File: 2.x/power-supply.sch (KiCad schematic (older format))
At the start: 46 parts, among them Q29 BC846, Q30 MOSFET_P, Q31 BSS138, U6 78L05, U7 AP1117IE33G, U8 ZXCT1107SA-7, U9 ZXCT1107SA-7

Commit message: Added RGB output and finished power supply monitor schematic, including new current monitor and voltage monitor divider values.
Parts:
- removed R128, R129, R131, R132, R133: R, ~, symbol R
- removed U9: ZXCT1107SA-7, symbol ZXCT1107SA-7
- added U9: ZXCT1086E5TA, ~, symbol ZXCT1086E5TA
- D35: value VSOL -> LED
- D36: value 12V -> LED
- D37: value 5V -> LED
- D38: value 3.3V -> LED
- Q30: value MOSFET_P -> FDD5614P
- R115: value R -> 20.5K 1%
- R116: value R -> 0.075; Digikey P/N (none) -> 989-1030-1-ND
- R117, R118, R125: value R -> 5.1K 1%
- R122: value R -> 10K
- R124: value R -> 95.3K 1%
- R127: value R -> 18K
- R128: renamed from R130; value R -> .003
- R129: renamed from R134; value R -> 95.3K 1%
- R130: renamed from R135; value R -> 5.1K 1%
- renumbered R136 to R131, R137 to R132, R138 to R133, R139 to R134
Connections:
- net labels added: RGB_12V_OUT
- wire segments 106 -> 142
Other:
- note added: "LRC-LR1206LF-01-R075F"

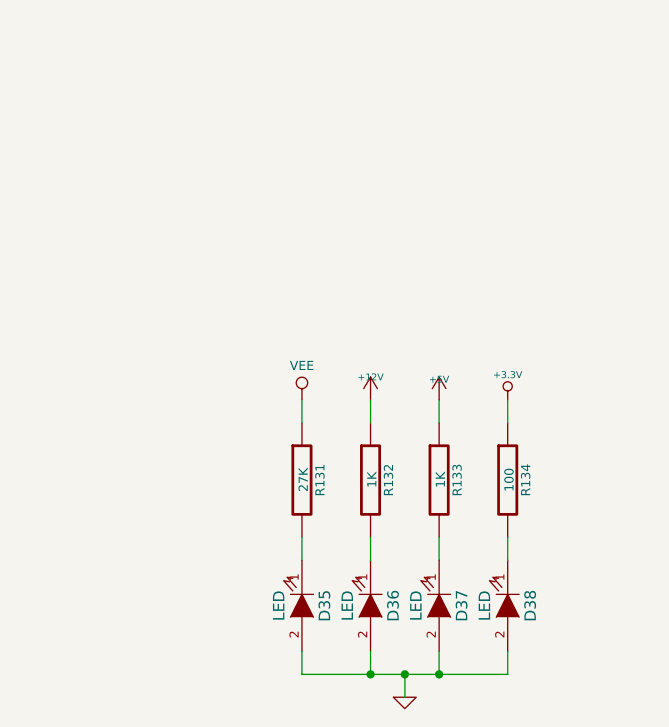
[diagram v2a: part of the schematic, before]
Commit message: Cleaning up schematic Updating solenoid driver to use 12V for MOSFET gates instead of Vsol so we never exceed Vgs_max
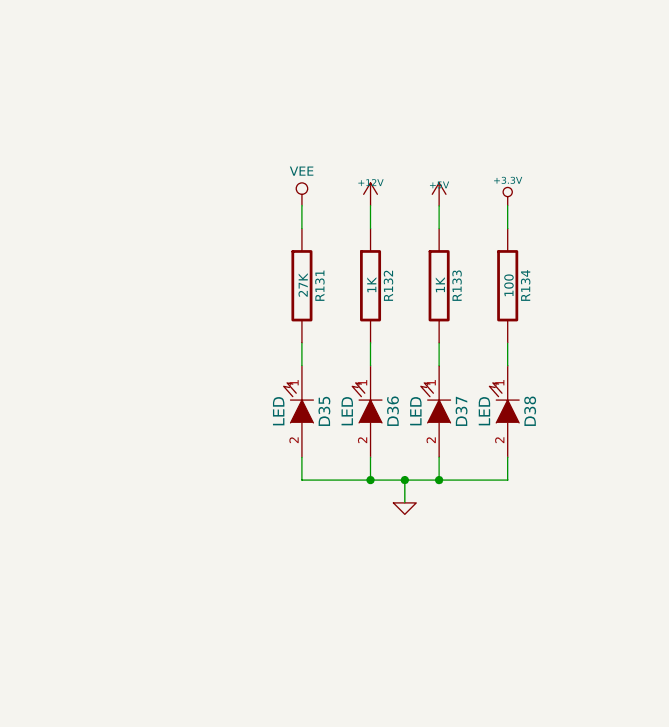
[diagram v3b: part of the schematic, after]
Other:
- moved on the sheet: D35, D36, D37, D38, R131, R132, R133, R134
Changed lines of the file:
@@
 LIBS:nxp_armmcu
 LIBS:base-module-hardware-v2-cache
-EELAYER 27 0
+EELAYER 25 0
 EELAYER END
 $Descr USLetter 11000 8500
@@
 L R R131
 U 1 1 5323DD09
-P 9100 6200
-F 0 "R131" V 9180 6200 40  0000 C CNN
-F 1 "27K" V 9107 6201 40  0000 C CNN
-F 2 "~" V 9030 6200 30  0000 C CNN
-F 3 "~" H 9100 6200 30  0000 C CNN
-	1    9100 6200
+P 9100 5350
+F 0 "R131" V 9180 5350 40  0000 C CNN
+F 1 "27K" V 9107 5351 40  0000 C CNN
+F 2 "~" V 9030 5350 30  0000 C CNN
+F 3 "~" H 9100 5350 30  0000 C CNN
+	1    9100 5350
 	1    0    0    -1
 $EndComp
@@
 L R R132
 U 1 1 5323DD18
-P 9400 6200
-F 0 "R132" V 9480 6200 40  0000 C CNN
-F 1 "1K" V 9407 6201 40  0000 C CNN
-F 2 "~" V 9330 6200 30  0000 C CNN
-F 3 "~" H 9400 6200 30  0000 C CNN
-	1    9400 6200
+P 9400 5350
+F 0 "R132" V 9480 5350 40  0000 C CNN
+F 1 "1K" V 9407 5351 40  0000 C CNN
+F 2 "~" V 9330 5350 30  0000 C CNN
+F 3 "~" H 9400 5350 30  0000 C CNN
+	1    9400 5350
 	1    0    0    -1
 $EndComp
@@
 L R R133
 U 1 1 5323DD27
-P 9700 6200
-F 0 "R133" V 9780 6200 40  0000 C CNN
-F 1 "1K" V 9707 6201 40  0000 C CNN
-F 2 "~" V 9630 6200 30  0000 C CNN
-F 3 "~" H 9700 6200 30  0000 C CNN
-	1    9700 6200
+P 9700 5350
+F 0 "R133" V 9780 5350 40  0000 C CNN
+F 1 "1K" V 9707 5351 40  0000 C CNN
+F 2 "~" V 9630 5350 30  0000 C CNN
+F 3 "~" H 9700 5350 30  0000 C CNN
+	1    9700 5350
 	1    0    0    -1
 $EndComp
@@
 L R R134
 U 1 1 5323DD36
-P 10000 6200
-F 0 "R134" V 10080 6200 40  0000 C CNN
-F 1 "100" V 10007 6201 40  0000 C CNN
-F 2 "~" V 9930 6200 30  0000 C CNN
-F 3 "~" H 10000 6200 30  0000 C CNN
-	1    10000 6200
+P 10000 5350
+F 0 "R134" V 10080 5350 40  0000 C CNN
+F 1 "100" V 10007 5351 40  0000 C CNN
+F 2 "~" V 9930 5350 30  0000 C CNN
+F 3 "~" H 10000 5350 30  0000 C CNN
+	1    10000 5350
 	1    0    0    -1
 $EndComp
@@
 L LED D36
 U 1 1 5323DD59
-P 9400 6750
-F 0 "D36" H 9400 6850 50  0000 C CNN
-F 1 "LED" H 9400 6650 50  0000 C CNN
-F 2 "~" H 9400 6750 60  0000 C CNN
-F 3 "~" H 9400 6750 60  0000 C CNN
-	1    9400 6750
+P 9400 5900
+F 0 "D36" H 9400 6000 50  0000 C CNN
+F 1 "LED" H 9400 5800 50  0000 C CNN
+F 2 "~" H 9400 5900 60  0000 C CNN
+F 3 "~" H 9400 5900 60  0000 C CNN
+	1    9400 5900
 	0    1    1    0
 $EndComp
@@
 L LED D35
 U 1 1 5323DD68
-P 9100 6750
-F 0 "D35" H 9100 6850 50  0000 C CNN
-F 1 "LED" H 9100 6650 50  0000 C CNN
-F 2 "~" H 9100 6750 60  0000 C CNN
-F 3 "~" H 9100 6750 60  0000 C CNN
-	1    9100 6750
+P 9100 5900
+F 0 "D35" H 9100 6000 50  0000 C CNN
+F 1 "LED" H 9100 5800 50  0000 C CNN
+F 2 "~" H 9100 5900 60  0000 C CNN
+F 3 "~" H 9100 5900 60  0000 C CNN
+	1    9100 5900
 	0    1    1    0
 $EndComp
@@
 L LED D37
 U 1 1 5323DD77
-P 9700 6750
-F 0 "D37" H 9700 6850 50  0000 C CNN
-F 1 "LED" H 9700 6650 50  0000 C CNN
-F 2 "~" H 9700 6750 60  0000 C CNN
-F 3 "~" H 9700 6750 60  0000 C CNN
-	1    9700 6750
+P 9700 5900
+F 0 "D37" H 9700 6000 50  0000 C CNN
+F 1 "LED" H 9700 5800 50  0000 C CNN
+F 2 "~" H 9700 5900 60  0000 C CNN
+F 3 "~" H 9700 5900 60  0000 C CNN
+	1    9700 5900
 	0    1    1    0
 $EndComp
@@
 L LED D38
 U 1 1 5323DD86
-P 10000 6750
-F 0 "D38" H 10000 6850 50  0000 C CNN
-F 1 "LED" H 10000 6650 50  0000 C CNN
-F 2 "~" H 10000 6750 60  0000 C CNN
-F 3 "~" H 10000 6750 60  0000 C CNN
-	1    10000 6750
+P 10000 5900
+F 0 "D38" H 10000 6000 50  0000 C CNN
+F 1 "LED" H 10000 5800 50  0000 C CNN
+F 2 "~" H 10000 5900 60  0000 C CNN
+F 3 "~" H 10000 5900 60  0000 C CNN
+	1    10000 5900
 	0    1    1    0
 $EndComp
 Wire Wire Line
-	9100 6450 9100 6550
-Wire Wire Line
-	9400 6550 9400 6450
-Wire Wire Line
-	9700 6450 9700 6550
-Wire Wire Line
-	10000 6550 10000 6450
-Wire Wire Line
-	9100 6950 9100 7050
-Wire Wire Line
-	9100 7050 9400 7050
-Wire Wire Line
-	9400 7050 9550 7050
-Wire Wire Line
-	9550 7050 9700 7050
-Wire Wire Line
-	9700 7050 10000 7050
-Wire Wire Line
-	10000 7050 10000 6950
-Wire Wire Line
-	9700 6950 9700 7050
-Connection ~ 9700 7050
-Wire Wire Line
-	9400 6950 9400 7050
-Connection ~ 9400 7050
+	9100 5600 9100 5700
+Wire Wire Line
+	9400 5700 9400 5600
+Wire Wire Line
+	9700 5600 9700 5700
+Wire Wire Line
+	10000 5700 10000 5600
+Wire Wire Line
+	9100 6100 9100 6200
+Wire Wire Line
+	9100 6200 9400 6200
+Wire Wire Line
+	9400 6200 9550 6200
+Wire Wire Line
+	9550 6200 9700 6200
+Wire Wire Line
+	9700 6200 10000 6200
+Wire Wire Line
+	10000 6200 10000 6100
+Wire Wire Line
+	9700 6100 9700 6200
+Connection ~ 9700 6200
+Wire Wire Line
+	9400 6100 9400 6200
+Connection ~ 9400 6200
 $Comp
 L GND #PWR57
 U 1 1 5323DED8
-P 9550 7150
-F 0 "#PWR57" H 9550 7150 30  0001 C CNN
-F 1 "GND" H 9550 7080 30  0001 C CNN
-F 2 "" H 9550 7150 60  0000 C CNN
-F 3 "" H 9550 7150 60  0000 C CNN
-	1    9550 7150
-	1    0    0    -1
-$EndComp
-Wire Wire Line
-	9550 7150 9550 7050
-Connection ~ 9550 7050
+P 9550 6300
+F 0 "#PWR57" H 9550 6300 30  0001 C CNN
+F 1 "GND" H 9550 6230 30  0001 C CNN
+F 2 "" H 9550 6300 60  0000 C CNN
+F 3 "" H 9550 6300 60  0000 C CNN
+	1    9550 6300
+	1    0    0    -1
+$EndComp
+Wire Wire Line
+	9550 6300 9550 6200
+Connection ~ 9550 6200
 $Comp
 L +3.3V #PWR59
 U 1 1 5323DF0D
-P 10000 5850
-F 0 "#PWR59" H 10000 5810 30  0001 C CNN
-F 1 "+3.3V" H 10000 5960 30  0000 C CNN
-F 2 "" H 10000 5850 60  0000 C CNN
-F 3 "" H 10000 5850 60  0000 C CNN
-	1    10000 5850
+P 10000 5000
+F 0 "#PWR59" H 10000 4960 30  0001 C CNN
+F 1 "+3.3V" H 10000 5110 30  0000 C CNN
+F 2 "" H 10000 5000 60  0000 C CNN
+F 3 "" H 10000 5000 60  0000 C CNN
+	1    10000 5000
 	1    0    0    -1
 $EndComp
@@
 L +5V #PWR58
 U 1 1 5323DF1C
-P 9700 5850
-F 0 "#PWR58" H 9700 5940 20  0001 C CNN
-F 1 "+5V" H 9700 5940 30  0000 C CNN
-F 2 "" H 9700 5850 60  0000 C CNN
-F 3 "" H 9700 5850 60  0000 C CNN
-	1    9700 5850
+P 9700 5000
+F 0 "#PWR58" H 9700 5090 20  0001 C CNN
+F 1 "+5V" H 9700 5090 30  0000 C CNN
+F 2 "" H 9700 5000 60  0000 C CNN
+F 3 "" H 9700 5000 60  0000 C CNN
+	1    9700 5000
 	1    0    0    -1
 $EndComp
@@
 L +12V #PWR56
 U 1 1 5323DF2B
-P 9400 5850
-F 0 "#PWR56" H 9400 5800 20  0001 C CNN
-F 1 "+12V" H 9400 5950 30  0000 C CNN
-F 2 "" H 9400 5850 60  0000 C CNN
-F 3 "" H 9400 5850 60  0000 C CNN
-	1    9400 5850
-	1    0    0    -1
-$EndComp
-Wire Wire Line
-	9400 5850 9400 5950
-Wire Wire Line
-	9700 5850 9700 5950
-Wire Wire Line
-	10000 5850 10000 5950
+P 9400 5000
+F 0 "#PWR56" H 9400 4950 20  0001 C CNN
+F 1 "+12V" H 9400 5100 30  0000 C CNN
+F 2 "" H 9400 5000 60  0000 C CNN
+F 3 "" H 9400 5000 60  0000 C CNN
+	1    9400 5000
+	1    0    0    -1
+$EndComp
+Wire Wire Line
+	9400 5000 9400 5100
+Wire Wire Line
+	9700 5000 9700 5100
+Wire Wire Line
+	10000 5000 10000 5100
 $Comp
 L VEE #PWR53
 U 1 1 5323DFC9
-P 9100 5850
-F 0 "#PWR53" H 9100 6050 40  0001 C CNN
-F 1 "VEE" H 9100 6000 40  0000 C CNN
-F 2 "" H 9100 5850 60  0000 C CNN
-F 3 "" H 9100 5850 60  0000 C CNN
-	1    9100 5850
-	1    0    0    -1
-$EndComp
-Wire Wire Line
-	9100 5850 9100 5950
+P 9100 5000
+F 0 "#PWR53" H 9100 5200 40  0001 C CNN
+F 1 "VEE" H 9100 5150 40  0000 C CNN
+F 2 "" H 9100 5000 60  0000 C CNN
+F 3 "" H 9100 5000 60  0000 C CNN
+	1    9100 5000
+	1    0    0    -1
+$EndComp
+Wire Wire Line
+	9100 5000 9100 5100
 Text HLabel 3600 3100 2    60   Output ~ 0
 SWITCH_12V_OUT

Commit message: Started layout on 2.0
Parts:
- removed U6: 78L05, ~, symbol 78L05
- added U4: MC78L05ACH, SMD_Packages:SOT-223, symbol MC78L05ACH
- C13: renamed from C15; footprint ~ -> Capacitors_SMD:C_0805
- C14: renamed from C18; footprint ~ -> Capacitors_SMD:C_0805
- C15: renamed from C21; footprint ~ -> Capacitors_SMD:C_0805
- C16: footprint ~ -> Capacitors_SMD:C_0805
- C17: renamed from C19; footprint ~ -> Capacitors_SMD:C_0603
- C18: renamed from C20; footprint ~ -> Capacitors_ThroughHole:C_Radial_D16_L25_P7.5
- C19: renamed from C22; footprint ~ -> Capacitors_SMD:C_0805
- C20: renamed from C17; footprint ~ -> Capacitors_SMD:C_0805
- D35, D36, D37, D38: footprint ~ -> LEDs:LED-0603
- F1, F2: footprint ~ -> PinballParts:FC203-20MM
- Q29: renamed from Q31; footprint SOT-23 -> Housings_SOT-23_SOT-143_TSOT-6:SOT-23
- Q30: footprint ~ -> PinballParts:DPAK-2
- Q31: renamed from Q29; footprint SOT-23 -> Housings_SOT-23_SOT-143_TSOT-6:SOT-23
- R115: renamed from R119; footprint ~ -> Resistors_SMD:R_0603
- R116: renamed from R120; footprint ~ -> Resistors_SMD:R_0603
- R117: renamed from R124; footprint ~ -> Resistors_SMD:R_0603
- R118: renamed from R125; footprint ~ -> Resistors_SMD:R_0603
- R119: renamed from R128; footprint ~ -> Resistors_SMD:R_1206; Digikey P/N (none) -> 989-1026-1-ND
- R120: renamed from R129; footprint ~ -> Resistors_SMD:R_0603
- R121: renamed from R122; footprint ~ -> Resistors_SMD:R_0603
- R122: renamed from R126; footprint ~ -> Resistors_SMD:R_0603
- R123: renamed from R130; footprint ~ -> Resistors_SMD:R_0603
- R124: renamed from R116; footprint ~ -> Resistors_SMD:R_1206
- R125: renamed from R127; value 18K -> 27K; footprint ~ -> Resistors_SMD:R_0603
- R126: renamed from R121; footprint ~ -> Resistors_SMD:R_0603
- R127: renamed from R123; footprint ~ -> Resistors_SMD:R_0603
- R128: renamed from R117; footprint ~ -> Resistors_SMD:R_0603
- R129: renamed from R115; footprint ~ -> Resistors_SMD:R_0603
- R130: renamed from R131; footprint ~ -> Resistors_SMD:R_0603
- R131: renamed from R132; value 1K -> 2.7K; footprint ~ -> Resistors_SMD:R_0603
- R132: renamed from R133; footprint ~ -> Resistors_SMD:R_0603
- R133: renamed from R134; value 100 -> 1K; footprint ~ -> Resistors_SMD:R_0603
- R134: renamed from R118; footprint ~ -> Resistors_SMD:R_0603
- U5: renamed from U7; footprint ~ -> SMD_Packages:SOT-223
- U6: renamed from U9; footprint ~ -> Housings_SOT-23_SOT-143_TSOT-6:SOT-23-5
- U7: renamed from U8; footprint (none) -> Housings_SOT-23_SOT-143_TSOT-6:SOT-23
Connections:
- net labels added: SOL_12V_OUT
- wire segments 142 -> 103
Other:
- moved on the sheet: C20, R124, R128, R129, R134, U7

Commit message: Fixing BAT54C pinout, and some feedback from layout review.
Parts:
- removed R122: 22, Resistors_SMD:R_0603, symbol R
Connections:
- net at Q30.G: now also R121.2, R125.1
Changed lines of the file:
@@
-$EndComp
-$Comp
-L R R122
-U 1 1 53260007
-P 7050 2650
-F 0 "R122" V 7130 2650 40  0000 C CNN
-F 1 "22" V 7057 2651 40  0000 C CNN
-F 2 "Resistors_SMD:R_0603" V 6980 2650 30  0000 C CNN
-F 3 "~" H 7050 2650 30  0000 C CNN
-	1    7050 2650
-	1    0    0    -1
 $EndComp
 $Comp
@@
 	6050 3800 5850 3800
 Wire Wire Line
-	7050 2900 7050 3000
+	7050 2300 7050 3000
 Wire Wire Line
 	7050 2950 6550 2950
@@
 	6550 1400 6550 2400
 Connection ~ 6550 2000
-Wire Wire Line
-	7050 2400 7050 2300
 $Comp
 L R R127

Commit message: Finishing layout updates from review with Mike.
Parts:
- removed U4: MC78L05ACH, SMD_Packages:SOT-223, symbol MC78L05ACH
- removed U5: AP1117IE33G, SMD_Packages:SOT-223, symbol NCP1117ST33T3G
- added U4: MC78L05, SMD_Packages:SOT-223, symbol MC78L05
- added U5: AP1117IE33G, SMD_Packages:SOT-223, symbol AP1117IE33G
- C15: value 10u -> 10u DNP
- Q29: value BSS138 -> BSS138 DNP
- R115: value 1K -> 1K DNP
- R116: value 10K -> 10K DNP
- R117: value 95.3K 1% -> 95.3K 1% DNP
- R118: value 5.1K 1% -> 5.1K 1% DNP
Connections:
- net +12V: now also U4.3 (IN), U5.3 (VI)
- net +3.3V: now also U5.2 (VO), U5.4 (VO)
- net +5V: now also U4.1 (OUT)
- net GND: now also U4.2 (GND), U4.4 (GND), U5.1 (GND)
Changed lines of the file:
@@
 3V3_OUT
-$Comp
-L NCP1117ST33T3G U5
-U 1 1 5323D66C
-P 2900 2150
-F 0 "U5" H 3050 1954 40  0000 C CNN
-F 1 "AP1117IE33G" H 2900 2350 40  0000 C CNN
-F 2 "SMD_Packages:SOT-223" H 2900 2150 60  0001 C CNN
-F 3 "~" H 2900 2150 60  0000 C CNN
-	1    2900 2150
-	1    0    0    -1
-$EndComp
 $Comp
 L GND #PWR038
@@
 P 8450 1050
 F 0 "Q29" H 8450 901 40  0000 R CNN
-F 1 "BSS138" H 8450 1200 40  0000 R CNN
+F 1 "BSS138 DNP" H 8450 1200 40  0000 R CNN
 F 2 "Housings_SOT-23_SOT-143_TSOT-6:SOT-23" H 8320 1152 29  0000 C CNN
 F 3 "~" H 8450 1050 60  0000 C CNN
@@
 P 6200 950
 F 0 "R115" V 6280 950 40  0000 C CNN
-F 1 "1K" V 6207 951 40  0000 C CNN
+F 1 "1K DNP" V 6207 951 40  0000 C CNN
 F 2 "Resistors_SMD:R_0603" V 6130 950 30  0000 C CNN
 F 3 "~" H 6200 950 30  0000 C CNN
@@
 P 6200 1150
 F 0 "R116" V 6280 1150 40  0000 C CNN
-F 1 "10K" V 6207 1151 40  0000 C CNN
+F 1 "10K DNP" V 6207 1151 40  0000 C CNN
 F 2 "Resistors_SMD:R_0603" V 6130 1150 30  0000 C CNN
 F 3 "~" H 6200 1150 30  0000 C CNN
@@
 P 9200 1250
 F 0 "C15" H 9250 1350 40  0000 L CNN
-F 1 "10u" H 9250 1150 40  0000 L CNN
+F 1 "10u DNP" H 9250 1150 40  0000 L CNN
 F 2 "Capacitors_SMD:C_0805" H 9300 1100 30  0001 C CNN
 F 3 "~" H 9200 1250 300 0000 C CNN
@@
 P 7000 1400
 F 0 "R117" V 7080 1400 40  0000 C CNN
-F 1 "95.3K 1%" V 7007 1401 40  0000 C CNN
+F 1 "95.3K 1% DNP" V 7007 1401 40  0000 C CNN
 F 2 "Resistors_SMD:R_0603" V 6930 1400 30  0000 C CNN
 F 3 "~" H 7000 1400 30  0000 C CNN
@@
 P 7000 1600
 F 0 "R118" V 7080 1600 40  0000 C CNN
-F 1 "5.1K 1%" V 7007 1601 40  0000 C CNN
+F 1 "5.1K 1% DNP" V 7007 1601 40  0000 C CNN
 F 2 "Resistors_SMD:R_0603" V 6930 1600 30  0000 C CNN
 F 3 "~" H 7000 1600 30  0000 C CNN
@@
 Connection ~ 2100 2950
 $Comp
-L MC78L05ACH U4
-U 1 1 556AB3B4
+L MC78L05 U4
+U 1 1 558D7698
 P 2900 1000
 F 0 "U4" H 2700 1200 40  0000 C CNN
-F 1 "MC78L05ACH" H 2900 1200 40  0000 L CNN
+F 1 "MC78L05" H 2900 1200 40  0000 L CNN
 F 2 "SMD_Packages:SOT-223" H 2900 1100 30  0000 C CIN
 F 3 "" H 2900 1000 60  0000 C CNN
@@
 	1    0    0    -1
 $EndComp
+Wire Wire Line
+	3000 1250 3000 1550
+Connection ~ 3000 1550
+$Comp
+L AP1117IE33G U5
+U 1 1 558D864C
+P 2900 2150
+F 0 "U5" H 2900 2400 40  0000 C CNN
+F 1 "AP1117IE33G" H 2900 2350 40  0000 C CNN
+F 2 "SMD_Packages:SOT-223" H 2900 2150 60  0000 C CNN
+F 3 "" H 2900 2150 60  0000 C CNN
+	1    2900 2150
+	1    0    0    -1
+$EndComp
+Wire Wire Line
+	3300 2200 3350 2200
+Wire Wire Line
+	3350 2200 3350 2100
+Connection ~ 3350 2100
 $EndSCHEMATC

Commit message: Committing latest files. This includes the KiCAD 4.0.0rc1 migration as well as the updates to Base Board 2.1.
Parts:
- removed C15: 10u DNP, Capacitors_SMD:C_0805, symbol CP
- removed Q29: BSS138 DNP, Housings_SOT-23_SOT-143_TSOT-6:SOT-23, symbol BSS138
- removed R115: 1K DNP, Resistors_SMD:R_0603, symbol R
- removed R116: 10K DNP, Resistors_SMD:R_0603, symbol R
- removed R117: 95.3K 1% DNP, Resistors_SMD:R_0603, symbol R
- removed R118: 5.1K 1% DNP, Resistors_SMD:R_0603, symbol R
- C13, C14, C16, C18, C19, C20: symbol CP -> CP-RESCUE-base-module-hardware-v2
- C17: symbol C -> C-RESCUE-base-module-hardware-v2
- R119, R120, R121, R123, R124, R125, R126, R127, R128, R129, R130, R131, R132, R133, R134: symbol R -> R-RESCUE-base-module-hardware-v2
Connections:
- net GND: now also D35.1 (K), D36.1 (K), D37.1 (K), D38.1 (K); no longer D35.2 (A), D36.2 (A), D37.2 (A), D38.2 (A)
- net at R130.2: now also D35.2 (A); no longer D35.1 (K)
- net at R131.2: now also D36.2 (A); no longer D36.1 (K)
- net at R132.2: now also D37.2 (A); no longer D37.1 (K)
- net at R133.2: now also D38.2 (A); no longer D38.1 (K)
